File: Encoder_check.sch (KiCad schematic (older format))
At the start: 18 parts, among them J1 Conn_01x08, J2 Conn_01x06, P1 Digital, P2 Analog, P3 CONN_01X01, P4 CONN_01X01, P5 CONN_01X01, P6 CONN_01X01, U1 AM26LV32xD, U2 ST490AB

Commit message: AW
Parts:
- removed C1, C2: C, Capacitor_SMD:C_0603_1608Metric, symbol Device:C
- removed J1: Conn_01x08, TerminalBlock_TE-Connectivity:TerminalBlock_TE_282834-8_1x08_P2.54mm_Horizontal, symbol Connector_Generic:Conn_01x08
- removed P3, P4, P5, P6: CONN_01X01, Socket_Arduino_Nano:1pin_Nano, symbol Connector_Generic:Conn_01x01
- removed U1: AM26LV32xD, Package_SO:SOIC-16_3.9x9.9mm_P1.27mm, symbol Interface:AM26LV32xD
- removed U2: ST490AB, Package_SO:SO-8_3.9x4.9mm_P1.27mm, symbol mylib:ST490AB
- added C14: 3.3u, Capacitor_SMD:C_0805_2012Metric, symbol Device:C
- added D10, D11: LED, LED_SMD:LED_0603_1608Metric, symbol Device:LED
- added D5, D6, D7: SK6805, LED_SMD:LED_SK6805_PLCC4_2.4x2.7mm_P1.3mm, symbol LED:SK6805
- added H1, H2, H3, H4: MountingHole, MountingHole:MountingHole_3.2mm_M3, symbol Mechanical:MountingHole
- added J1: Conn_01x10, Connector_Multicomp:Multicomp_MC9A12-1034_2x05_P2.54mm_Vertical, symbol Connector_Generic:Conn_01x10
- added J3: Conn_01x04, Connector_JST:JST_EH_S4B-EH_1x04_P2.50mm_Horizontal, symbol Connector_Generic:Conn_01x04
- added J4: Screw_Terminal_01x06, TerminalBlock_TE-Connectivity:TerminalBlock_TE_282834-6_1x06_P2.54mm_Horizontal, symbol Connector:Screw_Terminal_01x06
- added J6, J8: Screw_Terminal_01x02, TerminalBlock_Phoenix:TerminalBlock_Phoenix_MKDS-1,5-2-5.08_1x02_P5.08mm_Horizontal, symbol Connector:Screw_Terminal_01x02
- added J7: Barrel_Jack_Switch, Connector_BarrelJack:BarrelJack_Horizontal, symbol Connector:Barrel_Jack_Switch
- added J9: Screw_Terminal_01x04, TerminalBlock_TE-Connectivity:TerminalBlock_TE_282834-4_1x04_P2.54mm_Horizontal, symbol Connector:Screw_Terminal_01x04
- added Q1: BSS138, Package_TO_SOT_SMD:SOT-23, symbol Transistor_FET:BSS138
- added R23, R24: 10k, Resistor_SMD:R_0603_1608Metric, symbol Device:R
- added R25: 1k, Resistor_SMD:R_0603_1608Metric, symbol Device:R
- added R26, R27, R28: R, Resistor_SMD:R_0603_1608Metric, symbol Device:R
- added TC1: Thermocouple_PCB, Connector_Omega:Omega_PCC-SMP_1x2_P13.70mm_Horizontal, symbol mylib:Thermocouple_PCB
- added U5: M78AR05-1, Converter_DCDC_my:Converter_DCDC_MINIMAX_M78AR05-1_THT, symbol mylib:M78AR05-1
- added U8: TLP785, Package_DIP:DIP-4_W7.62mm, symbol Isolator:TLP785
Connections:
- net +3V3: now also Q1.1 (G), R23.1, R26.1
- net +5V: now also C14.1, D5.4 (VDD), D6.4 (VDD), D7.4 (VDD), J1.3 (Pin_3), J9.1 (Pin_1), R24.1, U5.3 (OUT)
- net 10(**/SS): now also D11.2 (A), R26.2, U8.4
- net 11(**/MOSI): now also Q1.2 (S), R23.2
- net GND: now also C14.2, D5.2 (VSS), D6.2 (VSS), D7.2 (VSS), J1.2 (Pin_2), J3.1 (Pin_1), J7.2, J9.4 (Pin_4), R27.2, R28.2, TC1.3 (MP), U5.2 (GND), U8.3
- net ssi_encoder/C_-: now reaches J2.3 (Pin_3)
- net ssi_encoder/C_+: now reaches J2.4 (Pin_4)
- net ssi_encoder/D_+: now reaches J2.6 (Pin_6)
- net ssi_encoder/D_-: now reaches J2.5 (Pin_5)
- new net: D5.1 (DOUT), D6.3 (DIN)
- new net: D5.3 (DIN), Q1.3 (D), R24.2
- new net: D6.1 (DOUT), D7.3 (DIN)
- new net: R25.1, U8.1
- new net: J9.3 (Pin_3), U8.2
- new net: J9.2 (Pin_2), R25.2
- new net: D10.1 (K), R27.1
- new net: D11.1 (K), R28.1
- new net +24V: D10.2 (A), J3.2 (Pin_2), J7.1, U5.1 (IN)
- new net brake/brake_+: J8.1 (Pin_1)
- new net brake/brake_-: J8.2 (Pin_2)
- new net inc_encoder/A+: J1.5 (Pin_5)
- new net inc_encoder/A-: J1.6 (Pin_6)
- new net inc_encoder/B+: J1.7 (Pin_7)
- new net inc_encoder/B-: J1.8 (Pin_8)
- new net inc_encoder/I+: J1.9 (Pin_9)
- new net inc_encoder/I-: J1.10 (Pin_10)
- new net rs485/RS485_+: J3.3 (Pin_3)
- new net rs485/RS485_-: J3.4 (Pin_4)
- new net thermocouple/T+: J6.2 (Pin_2), TC1.1 (+)
- new net thermocouple/T-: J6.1 (Pin_1), TC1.2 (-)
- new net utm/PULSE_OUT+: J4.5 (Pin_5)
- new net utm/PULSE_OUT-: J4.6 (Pin_6)
- new net utm/PWR+(24V): J4.1 (Pin_1)
- new net utm/PWR-(0V): J4.2 (Pin_2)
- new net utm/SIG_GND: J4.4 (Pin_4)
- new net utm/SIG_OUT: J4.3 (Pin_3)
- no-connect marks 7 -> 3
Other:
- note removed: "Holes"
- moved on the sheet: D1, D2, D3, R1, R2, R3

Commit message: これで発注
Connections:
- net +5V: now also J9.4 (Pin_4); no longer J9.1 (Pin_1)
- net GND: now also J9.1 (Pin_1); no longer J9.4 (Pin_4)
- net at U8.2: now also J9.2 (Pin_2); no longer J9.3 (Pin_3)
- net at R25.2: now also J9.3 (Pin_3); no longer J9.2 (Pin_2)
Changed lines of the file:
@@
 $EndComp
-Wire Wire Line
-	6800 5500 6900 5500
 Wire Wire Line
 	6900 5500 6900 5450
@@
 Wire Wire Line
 	6900 5650 6900 5600
-Wire Wire Line
-	6900 5600 6800 5600
 $Comp
 L Connector_Generic:Conn_01x10 J1
@@
 Wire Wire Line
 	8300 5450 8850 5450
-$Comp
-L Connector:Screw_Terminal_01x04 J9
-U 1 1 5EA47402
-P 6600 5500
-F 0 "J9" H 6518 5817 50  0000 C CNN
-F 1 "Screw_Terminal_01x04" H 6518 5726 50  0000 C CNN
-F 2 "TerminalBlock_TE-Connectivity:TerminalBlock_TE_282834-4_1x04_P2.54mm_Horizontal" H 6600 5500 50  0001 C CNN
-F 3 "~" H 6600 5500 50  0001 C CNN
-	1    6600 5500
-	-1   0    0    -1
-$EndComp
-Wire Wire Line
-	6800 5400 6950 5400
 Wire Wire Line
 	6950 5400 6950 5050
@@
 	1    0    0    -1
 $EndComp
+Wire Wire Line
+	6800 5400 6950 5400
+Wire Wire Line
+	6800 5500 6900 5500
+Wire Wire Line
+	6900 5600 6800 5600
+$Comp
+L Connector:Screw_Terminal_01x04 J9
+U 1 1 5EA47402
+P 6600 5600
+F 0 "J9" H 6518 5175 50  0000 C CNN
+F 1 "Screw_Terminal_01x04" H 6518 5266 50  0000 C CNN
+F 2 "TerminalBlock_TE-Connectivity:TerminalBlock_TE_282834-4_1x04_P2.54mm_Horizontal" H 6600 5600 50  0001 C CNN
+F 3 "~" H 6600 5600 50  0001 C CNN
+	1    6600 5600
+	-1   0    0    1
+$EndComp
 $EndSCHEMATC

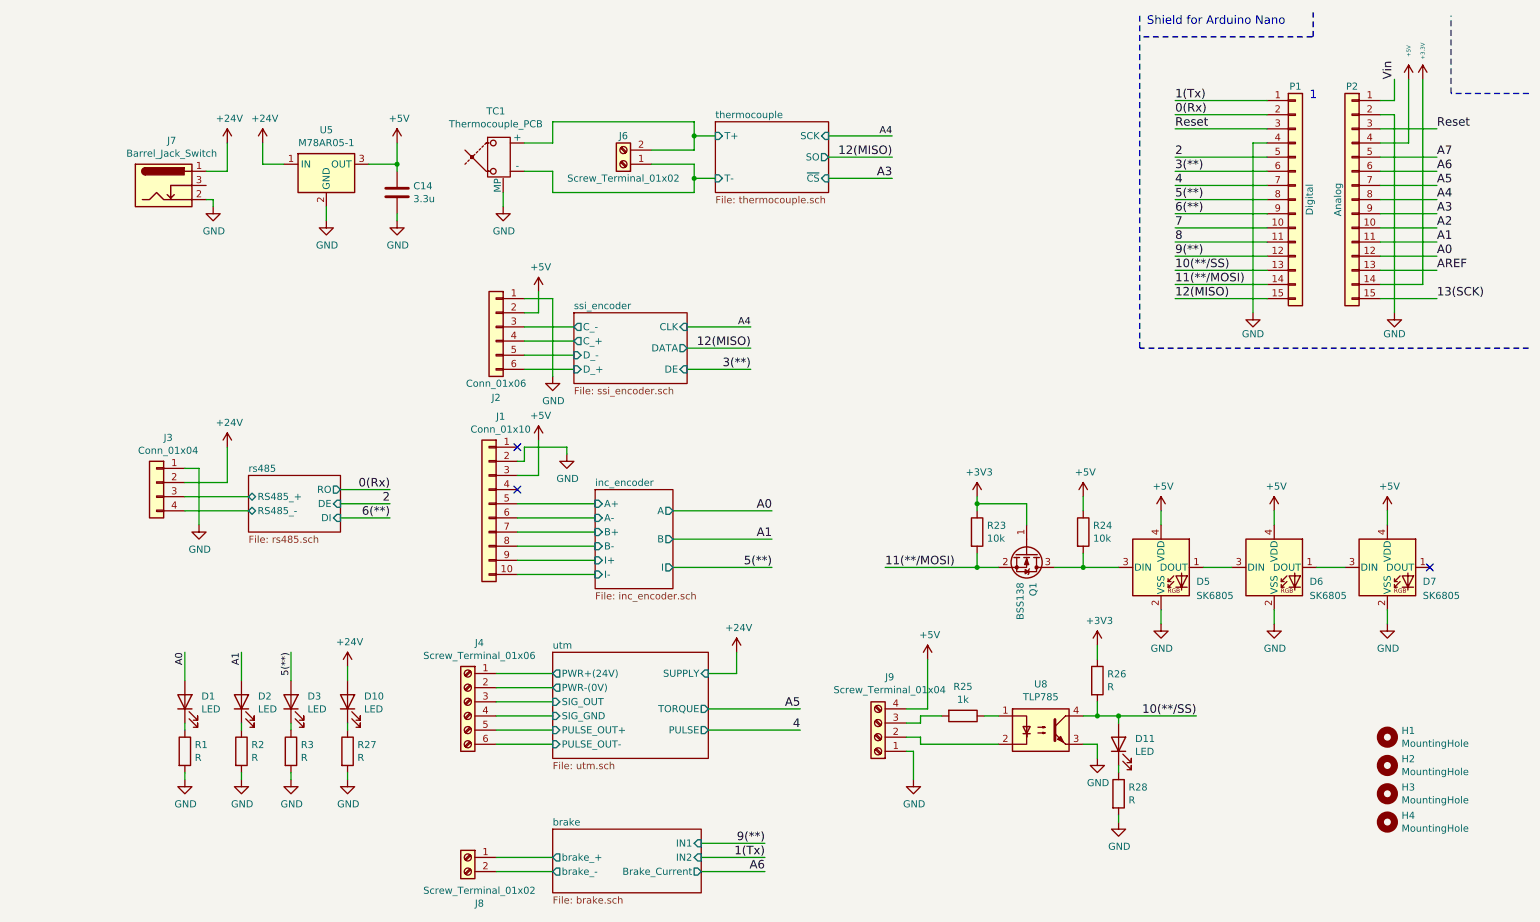
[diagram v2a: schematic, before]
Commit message: 見つけた設計ミスを全部反映
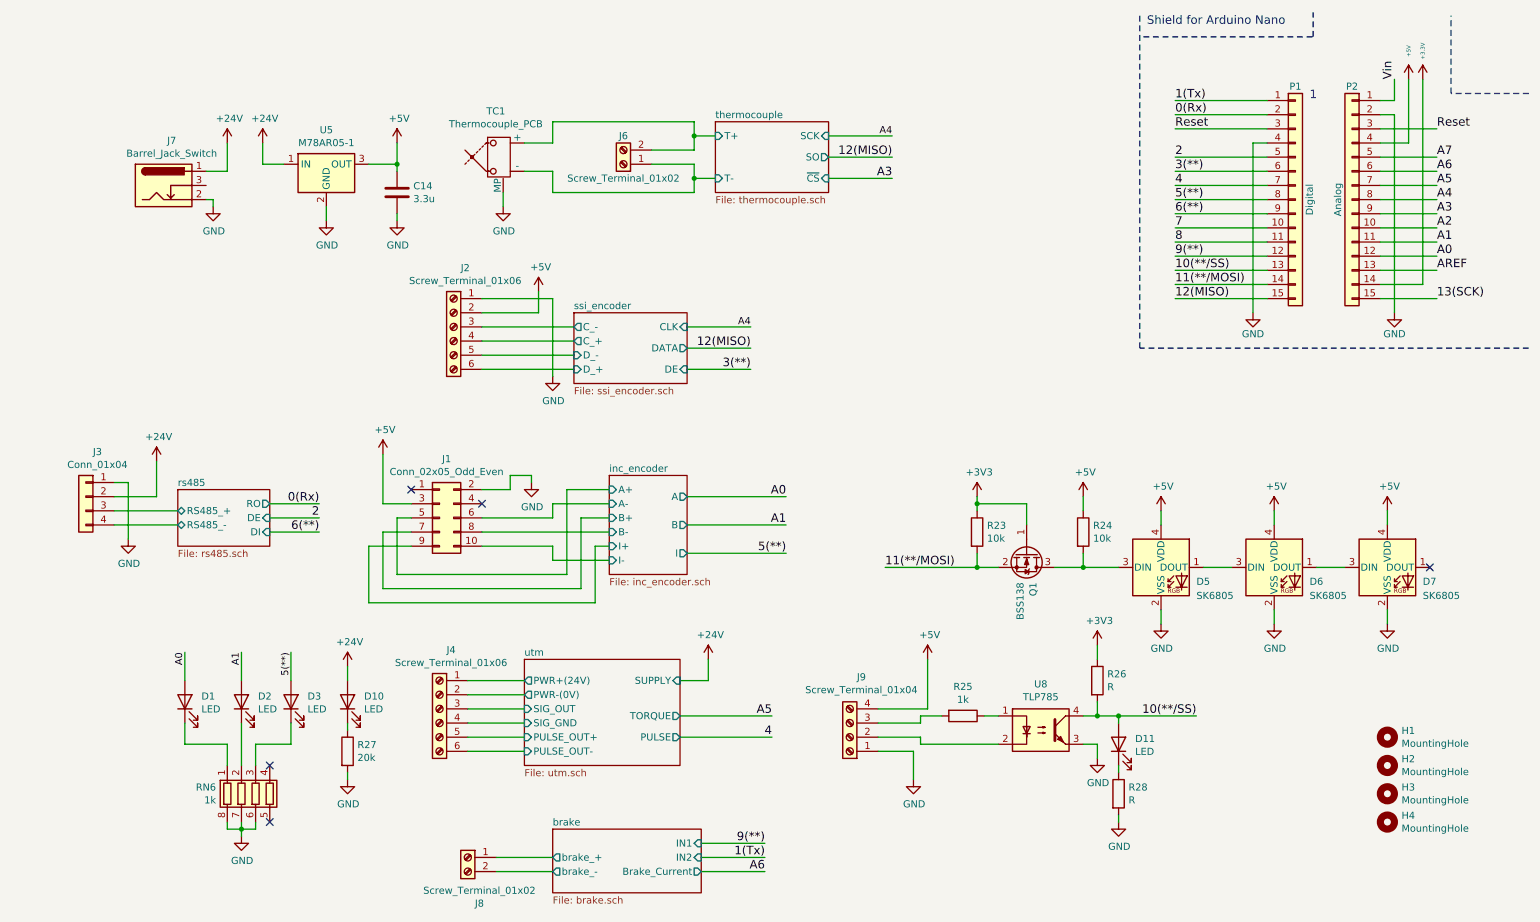
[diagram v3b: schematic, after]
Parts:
- removed J1: Conn_01x10, Connector_Multicomp:Multicomp_MC9A12-1034_2x05_P2.54mm_Vertical, symbol Connector_Generic:Conn_01x10
- removed J2: Conn_01x06, TerminalBlock_TE-Connectivity:TerminalBlock_TE_282834-6_1x06_P2.54mm_Horizontal, symbol Connector_Generic:Conn_01x06
- removed R1, R2, R3: R, Resistor_SMD:R_0603_1608Metric, symbol Device:R
- added J1: Conn_02x05_Odd_Even, Connector_Multicomp:Multicomp_MC9A12-1034_2x05_P2.54mm_Vertical, symbol Connector_Generic:Conn_02x05_Odd_Even
- added J2: Screw_Terminal_01x06, TerminalBlock_TE-Connectivity:TerminalBlock_TE_282834-6_1x06_P2.54mm_Horizontal, symbol Connector:Screw_Terminal_01x06
- added RN6: 1k, Resistor_SMD:R_Array_Concave_4x0603, symbol Device:R_Pack04
- R27: value R -> 20k
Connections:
- net +5V: now also J1.3 (Pin_3), J2.2 (Pin_2)
- net GND: now also J1.2 (Pin_2), J2.1 (Pin_1), RN6.6 (R3.2), RN6.7 (R2.2), RN6.8 (R1.2)
- net inc_encoder/A+: now also J1.5 (Pin_5)
- net inc_encoder/A-: now also J1.6 (Pin_6)
- net inc_encoder/B+: now also J1.7 (Pin_7)
- net inc_encoder/B-: now also J1.8 (Pin_8)
- net inc_encoder/I+: now also J1.9 (Pin_9)
- net inc_encoder/I-: now also J1.10 (Pin_10)
- net ssi_encoder/C_+: now also J2.4 (Pin_4)
- net ssi_encoder/C_-: now also J2.3 (Pin_3)
- net ssi_encoder/D_+: now also J2.6 (Pin_6)
- net ssi_encoder/D_-: now also J2.5 (Pin_5)
- net at D1.1 (K): now also RN6.1 (R1.1)
- net at D2.1 (K): now also RN6.2 (R2.1)
- net at D3.1 (K): now also RN6.3 (R3.1)
- no-connect marks 3 -> 5
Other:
- moved on the sheet: J3, J4, J9

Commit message: 部品のパラメータ未記入部分があったので追記
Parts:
- removed D11: LED, LED_SMD:LED_0603_1608Metric, symbol Device:LED
- removed R28: R, Resistor_SMD:R_0603_1608Metric, symbol Device:R
- added R1: 1k, Resistor_SMD:R_0603_1608Metric, symbol Device:R
- R26: value R -> 10k
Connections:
- net 10(**/SS): now also R1.1; no longer R26.2, U8.4
- new net: R1.2, R26.2, U8.4
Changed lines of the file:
@@
 	1    0    0    -1
 $EndComp
-Wire Wire Line
-	8150 5450 8300 5450
 Connection ~ 8150 5450
 Wire Wire Line
@@
 P 8150 5200
 F 0 "R26" H 8220 5246 50  0000 L CNN
-F 1 "R" H 8220 5155 50  0000 L CNN
+F 1 "10k" H 8220 5155 50  0000 L CNN
 F 2 "Resistor_SMD:R_0603_1608Metric" V 8080 5200 50  0001 C CNN
 F 3 "~" H 8150 5200 50  0001 C CNN
@@
 Wire Wire Line
 	8050 5450 8150 5450
-Text Label 8850 5450 2    60   ~ 0
+Text Label 9300 5450 2    60   ~ 0
 10(**/SS)
 $Comp
@@
 	1    0    0    -1
 $EndComp
-$Comp
-L Device:LED D11
-U 1 1 5E9F40E0
-P 8300 5650
-F 0 "D11" V 8339 5533 50  0000 R CNN
-F 1 "LED" V 8248 5533 50  0000 R CNN
-F 2 "LED_SMD:LED_0603_1608Metric" H 8300 5650 50  0001 C CNN
-F 3 "~" H 8300 5650 50  0001 C CNN
-	1    8300 5650
-	0    -1   -1   0
-$EndComp
-$Comp
-L Device:R R28
-U 1 1 5E9F40E6
-P 8300 6000
-F 0 "R28" H 8370 6046 50  0000 L CNN
-F 1 "R" H 8370 5955 50  0000 L CNN
-F 2 "Resistor_SMD:R_0603_1608Metric" V 8230 6000 50  0001 C CNN
-F 3 "~" H 8300 6000 50  0001 C CNN
-	1    8300 6000
-	1    0    0    -1
-$EndComp
-$Comp
-L power:GND #PWR0176
-U 1 1 5E9F40EC
-P 8300 6200
-F 0 "#PWR0176" H 8300 5950 50  0001 C CNN
-F 1 "GND" H 8305 6027 50  0000 C CNN
-F 2 "" H 8300 6200 50  0001 C CNN
-F 3 "" H 8300 6200 50  0001 C CNN
-	1    8300 6200
-	1    0    0    -1
-$EndComp
-Wire Wire Line
-	8300 6200 8300 6150
-Wire Wire Line
-	8300 5850 8300 5800
-Wire Wire Line
-	8300 5500 8300 5450
-Connection ~ 8300 5450
-Wire Wire Line
-	8300 5450 8850 5450
 Wire Wire Line
 	6950 5400 6950 5050
@@
 Wire Wire Line
 	1700 5500 1700 5650
+Wire Wire Line
+	8150 5450 8300 5450
+$Comp
+L Device:R R1
+U 1 1 5E5894D0
+P 8450 5450
+F 0 "R1" H 8520 5496 50  0000 L CNN
+F 1 "1k" H 8520 5405 50  0000 L CNN
+F 2 "Resistor_SMD:R_0603_1608Metric" V 8380 5450 50  0001 C CNN
+F 3 "~" H 8450 5450 50  0001 C CNN
+	1    8450 5450
+	0    1    1    0
+$EndComp
+Wire Wire Line
+	8600 5450 9300 5450
 $EndSCHEMATC

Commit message: エンコーダの配線ミスってた
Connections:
- net +5V: now also J1.2 (Pin_2); no longer J1.3 (Pin_3)
- net GND: now also J1.3 (Pin_3); no longer J1.2 (Pin_2)
- net inc_encoder/A+: now also J1.6 (Pin_6); no longer J1.5 (Pin_5)
- net inc_encoder/A-: now also J1.5 (Pin_5); no longer J1.6 (Pin_6)
- net inc_encoder/B+: now also J1.8 (Pin_8); no longer J1.7 (Pin_7)
- net inc_encoder/B-: now also J1.7 (Pin_7); no longer J1.8 (Pin_8)
- net inc_encoder/I+: now also J1.10 (Pin_10); no longer J1.9 (Pin_9)
- net inc_encoder/I-: now also J1.9 (Pin_9); no longer J1.10 (Pin_10)
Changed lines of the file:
@@
 $EndComp
-Wire Wire Line
-	3800 3850 4000 3850
-Wire Wire Line
-	4000 3850 4000 3750
 Wire Wire Line
 	4150 3750 4150 3800
-Wire Wire Line
-	3300 3950 3100 3950
 Wire Wire Line
 	6250 1650 6700 1650
@@
 Wire Wire Line
 	4000 3750 4150 3750
-Wire Wire Line
-	3100 3950 3100 3600
 $Comp
 L power:+5V #PWR0102
@@
 	-1   0    0    -1
 $EndComp
-$Comp
-L Connector_Generic:Conn_02x05_Odd_Even J1
-U 1 1 5E597057
-P 3500 4050
-F 0 "J1" H 3550 4467 50  0000 C CNN
-F 1 "Conn_02x05_Odd_Even" H 3550 4376 50  0000 C CNN
-F 2 "Connector_Multicomp:Multicomp_MC9A12-1034_2x05_P2.54mm_Vertical" H 3500 4050 50  0001 C CNN
-F 3 "~" H 3500 4050 50  0001 C CNN
-	1    3500 4050
-	1    0    0    -1
-$EndComp
-NoConn ~ 3300 3850
-NoConn ~ 3800 3950
+NoConn ~ 3300 3950
+NoConn ~ 3800 3850
 Wire Wire Line
 	3800 4150 4700 4150
@@
 	4400 4450 3200 4450
 Wire Wire Line
-	3200 4450 3200 4050
-Wire Wire Line
 	3200 4050 3300 4050
 Wire Wire Line
@@
 	3100 4550 3100 4150
 Wire Wire Line
-	3100 4150 3300 4150
-Wire Wire Line
 	4700 4250 4600 4250
 Wire Wire Line
@@
 Wire Wire Line
 	3000 4650 3000 4250
-Wire Wire Line
-	3000 4250 3300 4250
 $Comp
 L Device:R_Pack04 RN6
@@
 Wire Wire Line
 	8600 5450 9300 5450
+Wire Wire Line
+	3100 4150 3300 4150
+Wire Wire Line
+	3000 4250 3300 4250
+Wire Wire Line
+	3200 4450 3200 4050
+$Comp
+L Connector_Generic:Conn_02x05_Odd_Even J1
+U 1 1 5E597057
+P 3600 4050
+F 0 "J1" H 3650 4467 50  0000 C CNN
+F 1 "Conn_02x05_Odd_Even" H 3650 4376 50  0000 C CNN
+F 2 "Connector_Multicomp:Multicomp_MC9A12-1034_2x05_P2.54mm_Vertical" H 3600 4050 50  0001 C CNN
+F 3 "~" H 3600 4050 50  0001 C CNN
+	1    3600 4050
+	-1   0    0    -1
+$EndComp
+Wire Wire Line
+	3800 3950 4000 3950
+Wire Wire Line
+	4000 3750 4000 3950
+Wire Wire Line
+	3300 3850 3100 3850
+Wire Wire Line
+	3100 3850 3100 3600
 $EndSCHEMATC

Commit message: 設計修正
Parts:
- added J10: Conn_01x02, Connector_Amass:XT30PB, symbol Connector_Generic:Conn_01x02
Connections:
- net +24V: now also J10.1 (Pin_1)
- net GND: now also J10.2 (Pin_2)
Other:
- moved on the sheet: J7
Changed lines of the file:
@@
 L Connector:Barrel_Jack_Switch J7
 U 1 1 5E3DBA8B
-P 1550 1700
-F 0 "J7" H 1607 2017 50  0000 C CNN
-F 1 "Barrel_Jack_Switch" H 1607 1926 50  0000 C CNN
-F 2 "Connector_BarrelJack:BarrelJack_Horizontal" H 1600 1660 50  0001 C CNN
-F 3 "~" H 1600 1660 50  0001 C CNN
-	1    1550 1700
+P 850 1700
+F 0 "J7" H 907 2017 50  0000 C CNN
+F 1 "Barrel_Jack_Switch" H 907 1926 50  0000 C CNN
+F 2 "Connector_BarrelJack:BarrelJack_Horizontal" H 900 1660 50  0001 C CNN
+F 3 "~" H 900 1660 50  0001 C CNN
+	1    850  1700
 	1    0    0    -1
 $EndComp
@@
 L power:GND #PWR0146
 U 1 1 5E3DD04E
-P 1900 1850
-F 0 "#PWR0146" H 1900 1600 50  0001 C CNN
-F 1 "GND" H 1905 1677 50  0000 C CNN
-F 2 "" H 1900 1850 50  0001 C CNN
-F 3 "" H 1900 1850 50  0001 C CNN
-	1    1900 1850
-	1    0    0    -1
-$EndComp
-Wire Wire Line
-	1850 1800 1900 1800
-Wire Wire Line
-	1900 1800 1900 1850
+P 1200 1850
+F 0 "#PWR0146" H 1200 1600 50  0001 C CNN
+F 1 "GND" H 1205 1677 50  0000 C CNN
+F 2 "" H 1200 1850 50  0001 C CNN
+F 3 "" H 1200 1850 50  0001 C CNN
+	1    1200 1850
+	1    0    0    -1
+$EndComp
+Wire Wire Line
+	1150 1800 1200 1800
+Wire Wire Line
+	1200 1800 1200 1850
 $Comp
 L power:+24V #PWR0147
 U 1 1 5E3E14C7
-P 2000 1400
-F 0 "#PWR0147" H 2000 1250 50  0001 C CNN
-F 1 "+24V" H 2015 1573 50  0000 C CNN
-F 2 "" H 2000 1400 50  0001 C CNN
-F 3 "" H 2000 1400 50  0001 C CNN
-	1    2000 1400
-	1    0    0    -1
-$EndComp
-Wire Wire Line
-	1850 1600 2000 1600
-Wire Wire Line
-	2000 1600 2000 1400
+P 1300 1400
+F 0 "#PWR0147" H 1300 1250 50  0001 C CNN
+F 1 "+24V" H 1315 1573 50  0000 C CNN
+F 2 "" H 1300 1400 50  0001 C CNN
+F 3 "" H 1300 1400 50  0001 C CNN
+	1    1300 1400
+	1    0    0    -1
+$EndComp
+Wire Wire Line
+	1150 1600 1300 1600
+Wire Wire Line
+	1300 1600 1300 1400
 Wire Wire Line
 	3700 5700 4100 5700
@@
 Wire Wire Line
 	3100 3850 3100 3600
+$Comp
+L Connector_Generic:Conn_01x02 J10
+U 1 1 5E86F016
+P 1650 1650
+F 0 "J10" H 1568 1867 50  0000 C CNN
+F 1 "Conn_01x02" H 1568 1776 50  0000 C CNN
+F 2 "Connector_Amass:XT30PB" H 1650 1650 50  0001 C CNN
+F 3 "~" H 1650 1650 50  0001 C CNN
+	1    1650 1650
+	-1   0    0    -1
+$EndComp
+$Comp
+L power:+24V #PWR0116
+U 1 1 5E8877CC
+P 2000 1500
+F 0 "#PWR0116" H 2000 1350 50  0001 C CNN
+F 1 "+24V" H 2015 1673 50  0000 C CNN
+F 2 "" H 2000 1500 50  0001 C CNN
+F 3 "" H 2000 1500 50  0001 C CNN
+	1    2000 1500
+	1    0    0    -1
+$EndComp
+Wire Wire Line
+	1850 1650 2000 1650
+Wire Wire Line
+	2000 1650 2000 1500
+$Comp
+L power:GND #PWR0143
+U 1 1 5E893185
+P 2000 1900
+F 0 "#PWR0143" H 2000 1650 50  0001 C CNN
+F 1 "GND" H 2005 1727 50  0000 C CNN
+F 2 "" H 2000 1900 50  0001 C CNN
+F 3 "" H 2000 1900 50  0001 C CNN
+	1    2000 1900
+	1    0    0    -1
+$EndComp
+Wire Wire Line
+	2000 1750 2000 1900
+Wire Wire Line
+	1850 1750 2000 1750
 $EndSCHEMATC
